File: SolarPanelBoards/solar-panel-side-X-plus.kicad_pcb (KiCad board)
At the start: 2 copper layers, 82 x 99 mm, 43 parts, among them J1 Conn_01x06, Q12 BSS138DWQ-7, Q13 BSS138DWQ-7, Q7 MBT2222ADW1T1, Q8 MBT2222ADW1T1, U1 OPT3001DNPT

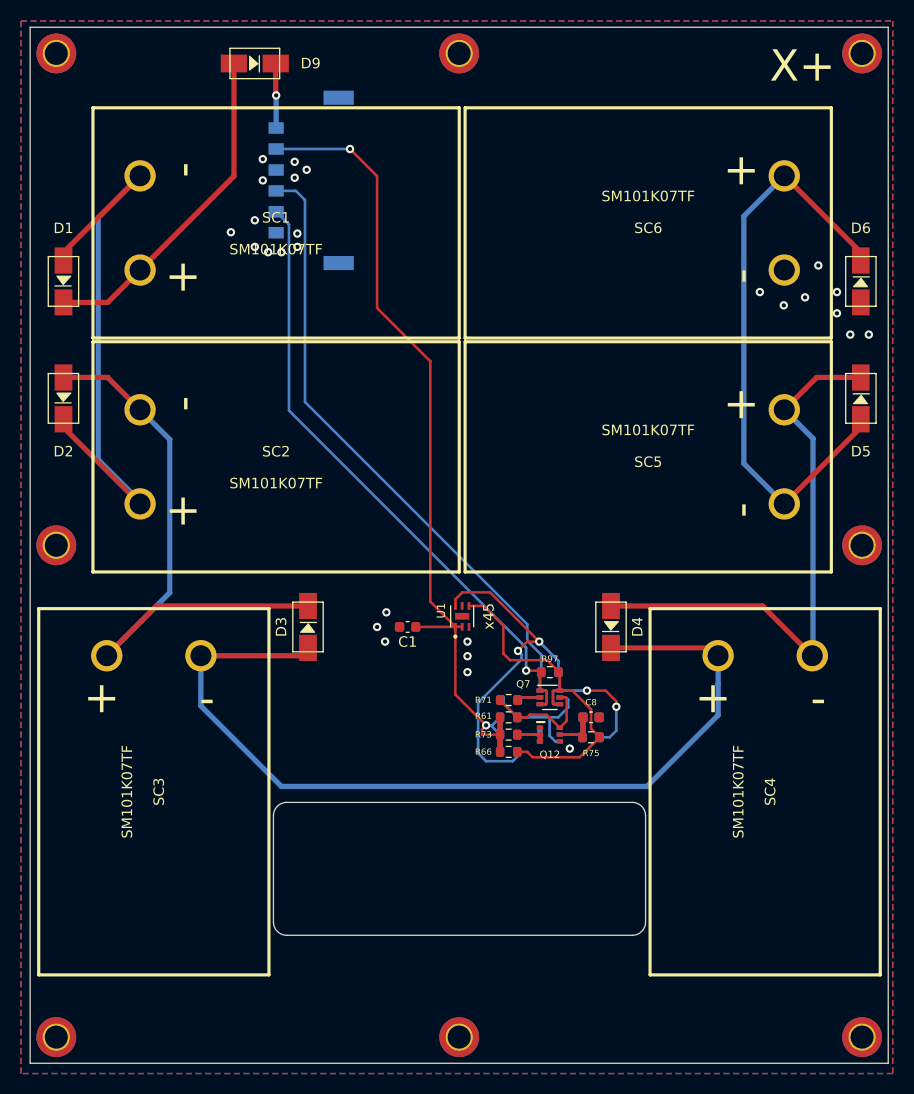
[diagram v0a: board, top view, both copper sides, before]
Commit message: Updated libraries and batteryboard/solarpanelboards accordingly
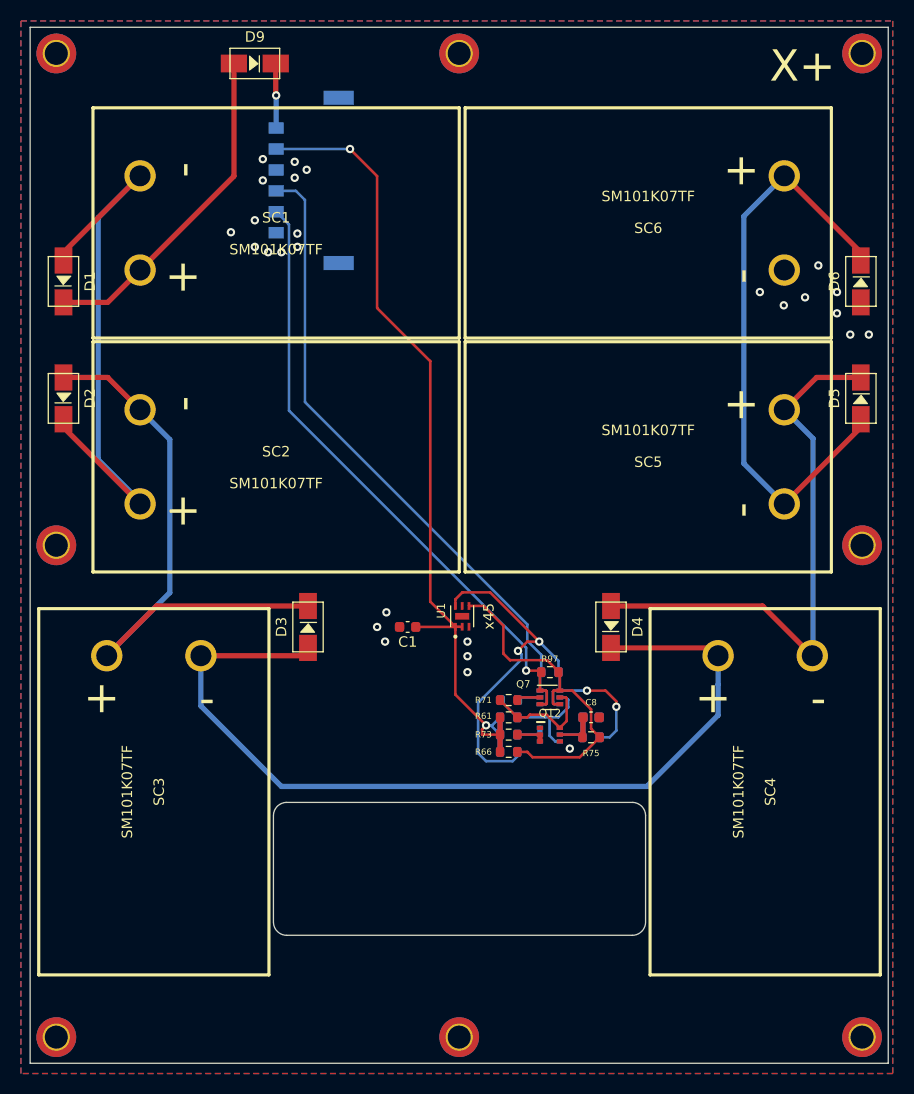
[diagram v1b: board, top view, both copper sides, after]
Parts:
- D1, D2, D3, D4, D5, D6, D9: footprint sapling:DO-214AC -> sputnik2U:DO-214AC
- J1: footprint sapling:MOLEX_2053380006 -> sputnik2U:MOLEX_2053380006
- Q12, Q13: footprint sapling:BSS138DWQ-7 -> sputnik2U:BSS138DWQ-7
- SC1, SC2, SC3, SC4, SC5, SC6: footprint sapling:SM101K07TF -> sputnik2U:SM101K07TF
- U1: footprint sapling:OPT3001 -> sputnik2U:OPT3001
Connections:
- J1 pad S1: (no net) -> unconnected-(J1-PadS1)
- J1 pad S2: (no net) -> unconnected-(J1-PadS2)
- U1 pad 5: (no net) -> unconnected-(U1-Pad5)

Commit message: Updated schematics, added/refined libraries
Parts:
- D1, D2, D3, D4, D5, D6, D9: footprint sputnik2U:DO-214AC -> panels:DO-214AC
- J1: footprint sputnik2U:MOLEX_2053380006 -> panels:MOLEX_2053380006
- Q12, Q13: footprint sputnik2U:BSS138DWQ-7 -> panels:BSS138DWQ-7
- SC1, SC2, SC3, SC4, SC5, SC6: footprint sputnik2U:SM101K07TF -> panels:SM101K07TF
- U1: footprint sputnik2U:OPT3001 -> panels:OPT3001
